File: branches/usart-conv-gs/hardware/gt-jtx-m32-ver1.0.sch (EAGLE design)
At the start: 29 parts, among them IC1 MEGA32-P

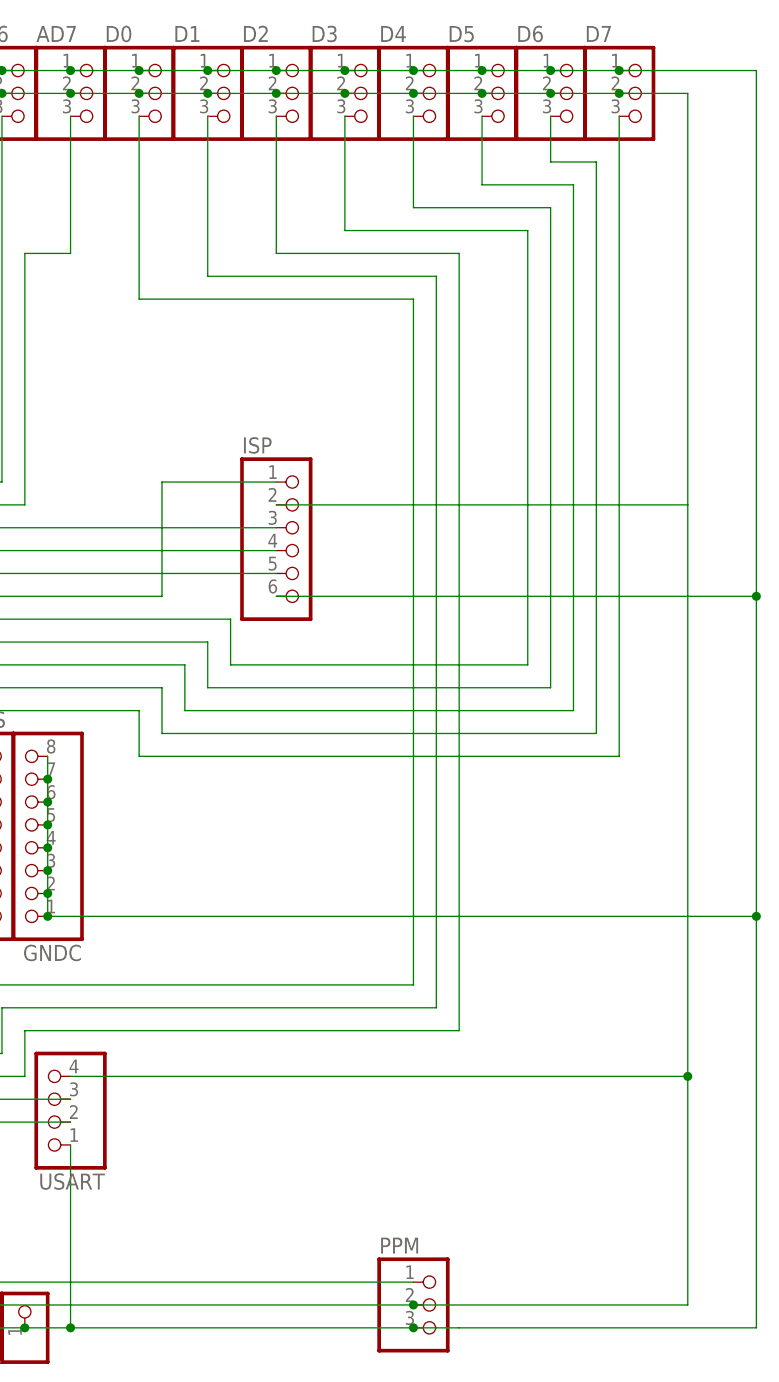
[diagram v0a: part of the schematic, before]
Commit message: changed pin header to 3x2 instead of 1x6 for accomodating a 6 pin isp. correctec pin configurations
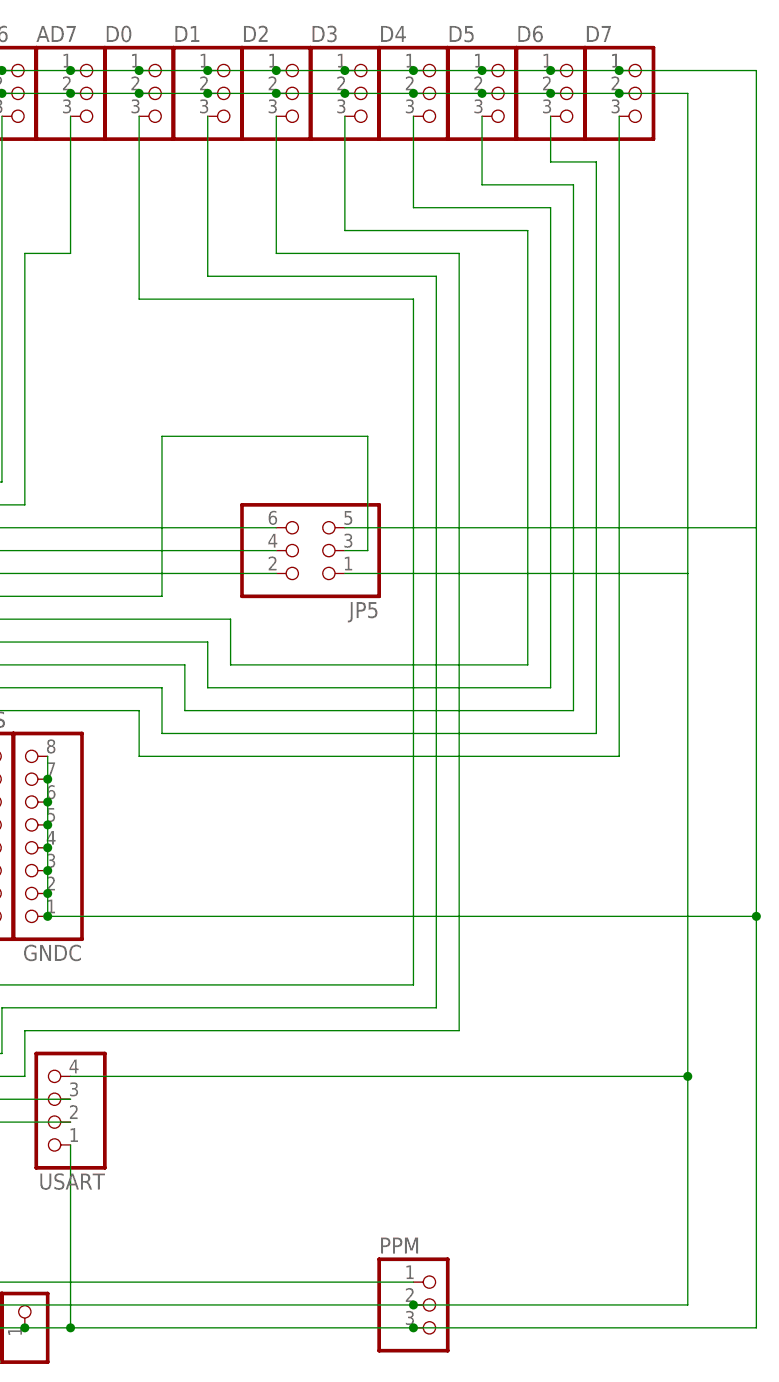
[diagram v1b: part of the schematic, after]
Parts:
- removed ISP: (no value), pinhead:PINHD-1X6
- added JP5: (no value), pinhead:PINHD-2X3
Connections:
- net +5V: now also JP5.1; no longer ISP.2
- net GND: now also JP5.5; no longer ISP.6
- net N$12: now also JP5.3; no longer ISP.1
- net N$13: now also JP5.2; no longer ISP.5
- net N$14: now also JP5.4; no longer ISP.4
- net N$9: now also JP5.6; no longer ISP.3
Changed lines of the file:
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@@
 <?xml version="1.0" encoding="utf-8"?>
 <!DOCTYPE eagle SYSTEM "eagle.dtd">
-<eagle version="6.3">
+<eagle version="7.5.0">
 <drawing>
 <settings>
@@
 <part name="R2" library="resistor" deviceset="R-US_" device="0204/2V"/>
 <part name="LED" library="led" deviceset="LED" device="5MM"/>
-<part name="ISP" library="pinhead" deviceset="PINHD-1X6" device=""/>
 <part name="IC1" library="atmel" deviceset="MEGA32-P" device=""/>
 <part name="USART" library="pinhead" deviceset="PINHD-1X4" device=""/>
@@
 <part name="JP3" library="pinhead" deviceset="PINHD-1X1" device=""/>
 <part name="JP4" library="pinhead" deviceset="PINHD-1X1" device=""/>
+<part name="JP5" library="pinhead" deviceset="PINHD-2X3" device=""/>
 </parts>
 <sheets>
@@
 <instance part="R2" gate="G$1" x="48.26" y="152.4"/>
 <instance part="LED" gate="G$1" x="38.1" y="139.7" rot="R270"/>
-<instance part="ISP" gate="A" x="160.02" y="129.54"/>
 <instance part="IC1" gate="G$1" x="91.44" y="109.22"/>
 <instance part="USART" gate="A" x="132.08" y="68.58" rot="R180"/>
@@
 <instance part="JP3" gate="G$1" x="124.46" y="45.72" rot="R90"/>
 <instance part="JP4" gate="G$1" x="129.54" y="45.72" rot="R90"/>
+<instance part="JP5" gate="A" x="162.56" y="129.54" rot="R180"/>
 </instances>
 <busses>
@@
 <wire x1="172.72" y1="45.72" x2="203.2" y2="45.72" width="0.1524" layer="91"/>
 <junction x="172.72" y="45.72"/>
-<wire x1="203.2" y1="71.12" x2="203.2" y2="134.62" width="0.1524" layer="91"/>
+<wire x1="203.2" y1="71.12" x2="203.2" y2="127" width="0.1524" layer="91"/>
 <pinref part="USART" gate="A" pin="4"/>
-<wire x1="203.2" y1="134.62" x2="203.2" y2="180.34" width="0.1524" layer="91"/>
+<wire x1="203.2" y1="127" x2="203.2" y2="180.34" width="0.1524" layer="91"/>
 <wire x1="203.2" y1="180.34" x2="195.58" y2="180.34" width="0.1524" layer="91"/>
 <wire x1="134.62" y1="71.12" x2="203.2" y2="71.12" width="0.1524" layer="91"/>
-<pinref part="ISP" gate="A" pin="2"/>
-<wire x1="157.48" y1="134.62" x2="203.2" y2="134.62" width="0.1524" layer="91"/>
 <pinref part="AD0" gate="A" pin="2"/>
 <pinref part="AD1" gate="A" pin="2"/>
@@
 <wire x1="203.2" y1="45.72" x2="203.2" y2="71.12" width="0.1524" layer="91"/>
 <junction x="203.2" y="71.12"/>
+<pinref part="JP5" gate="A" pin="1"/>
+<wire x1="165.1" y1="127" x2="203.2" y2="127" width="0.1524" layer="91"/>
 </segment>
 </net>
@@
 <pinref part="PPM" gate="A" pin="3"/>
 <wire x1="210.82" y1="43.18" x2="210.82" y2="88.9" width="0.1524" layer="91"/>
-<wire x1="210.82" y1="88.9" x2="210.82" y2="124.46" width="0.1524" layer="91"/>
-<wire x1="210.82" y1="124.46" x2="210.82" y2="182.88" width="0.1524" layer="91"/>
+<wire x1="210.82" y1="88.9" x2="210.82" y2="132.08" width="0.1524" layer="91"/>
+<wire x1="210.82" y1="132.08" x2="210.82" y2="182.88" width="0.1524" layer="91"/>
 <wire x1="132.08" y1="88.9" x2="210.82" y2="88.9" width="0.1524" layer="91"/>
 <junction x="210.82" y="88.9"/>
@@
 <wire x1="132.08" y1="104.14" x2="132.08" y2="106.68" width="0.1524" layer="91"/>
 <junction x="132.08" y="104.14"/>
-<pinref part="ISP" gate="A" pin="6"/>
-<wire x1="157.48" y1="124.46" x2="210.82" y2="124.46" width="0.1524" layer="91"/>
-<junction x="210.82" y="124.46"/>
 <pinref part="AD0" gate="A" pin="1"/>
 <pinref part="AD1" gate="A" pin="1"/>
@@
 <junction x="195.58" y="182.88"/>
 <wire x1="195.58" y1="182.88" x2="210.82" y2="182.88" width="0.1524" layer="91"/>
-<wire x1="175.26" y1="43.18" x2="177.8" y2="43.18" width="0.1524" layer="91"/>
-<wire x1="177.8" y1="43.18" x2="210.82" y2="43.18" width="0.1524" layer="91"/>
-<wire x1="175.26" y1="43.18" x2="172.72" y2="43.18" width="0.1524" layer="91"/>
+<wire x1="172.72" y1="43.18" x2="210.82" y2="43.18" width="0.1524" layer="91"/>
 <junction x="172.72" y="43.18"/>
 <pinref part="JP3" gate="G$1" pin="1"/>
@@
 <pinref part="JP4" gate="G$1" pin="1"/>
 <junction x="129.54" y="43.18"/>
+<pinref part="JP5" gate="A" pin="5"/>
+<wire x1="165.1" y1="132.08" x2="210.82" y2="132.08" width="0.1524" layer="91"/>
 </segment>
 </net>
@@
 <junction x="71.12" y="152.4"/>
 <wire x1="157.48" y1="132.08" x2="88.9" y2="132.08" width="0.1524" layer="91"/>
-<pinref part="ISP" gate="A" pin="3"/>
+<pinref part="JP5" gate="A" pin="6"/>
 </segment>
 </net>
@@
 <pinref part="IC1" gate="G$1" pin="(MISO)PB6"/>
 <wire x1="111.76" y1="127" x2="157.48" y2="127" width="0.1524" layer="91"/>
-<pinref part="ISP" gate="A" pin="5"/>
+<pinref part="JP5" gate="A" pin="2"/>
 </segment>
 </net>
@@
 <pinref part="IC1" gate="G$1" pin="(SCK)PB7"/>
 <wire x1="111.76" y1="129.54" x2="157.48" y2="129.54" width="0.1524" layer="91"/>
-<pinref part="ISP" gate="A" pin="4"/>
+<pinref part="JP5" gate="A" pin="4"/>
 </segment>
 </net>
@@
 <pinref part="IC1" gate="G$1" pin="(MOSI)PB5"/>
 <wire x1="111.76" y1="124.46" x2="144.78" y2="124.46" width="0.1524" layer="91"/>
-<wire x1="144.78" y1="124.46" x2="144.78" y2="137.16" width="0.1524" layer="91"/>
-<pinref part="ISP" gate="A" pin="1"/>
-<wire x1="144.78" y1="137.16" x2="157.48" y2="137.16" width="0.1524" layer="91"/>
-</segment>
-</net>
+<wire x1="144.78" y1="124.46" x2="144.78" y2="142.24" width="0.1524" layer="91"/>
+<wire x1="144.78" y1="142.24" x2="167.64" y2="142.24" width="0.1524" layer="91"/>
+<wire x1="167.64" y1="142.24" x2="167.64" y2="129.54" width="0.1524" layer="91"/>
+<pinref part="JP5" gate="A" pin="3"/>
+<wire x1="167.64" y1="129.54" x2="165.1" y2="129.54" width="0.1524" layer="91"/>
+</segment>
+</net>
